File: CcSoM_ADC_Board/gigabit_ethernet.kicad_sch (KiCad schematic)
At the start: 39 parts, among them J5 HR911130A1, U11 RTL8211E-VB-CG, Y1 25MHz

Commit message: changed schottky, began to add digikey part numbers
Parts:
- C1: DigiKey_no (none) -> 1276-CL05B104KP5VPNCCT-ND
- R39, R40: DigiKey_no (none) -> 2019-RK73B1ETTP511JCT-ND
- U11: DigiKey_no (none) -> 1188-SMDICRTL8211E-VB-CG-ND
- Y1: DigiKey_no (none) -> SER4211CT-ND
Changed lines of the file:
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@@
 			)
 		)
+		(property "DigiKey_no" "2019-RK73B1ETTP511JCT-ND"
+			(at 251.46 142.24 90)
+			(effects
+				(font
+					(size 1.27 1.27)
+				)
+				(hide yes)
+			)
+		)
 		(pin "1"
 		)
@@
 			)
 		)
+		(property "DigiKey_no" "SER4211CT-ND "
+			(at 140.97 168.91 90)
+			(effects
+				(font
+					(size 1.27 1.27)
+				)
+				(hide yes)
+			)
+		)
 		(pin "1"
 		)
@@
 			)
 		)
+		(property "DigiKey_no" "2019-RK73B1ETTP511JCT-ND"
+			(at 255.27 129.54 90)
+			(effects
+				(font
+					(size 1.27 1.27)
+				)
+				(hide yes)
+			)
+		)
 		(pin "1"
 		)
@@
 			)
 		)
+		(property "DigiKey_no" "1276-CL05B104KP5VPNCCT-ND"
+			(at 27.94 93.98 0)
+			(effects
+				(font
+					(size 1.27 1.27)
+				)
+				(hide yes)
+			)
+		)
 		(pin "1"
 		)
@@
 			(at 62.23 92.71 0)
 			(effects
+				(font
+					(size 1.27 1.27)
+				)
+				(hide yes)
+			)
+		)
+		(property "DigiKey_no" "1188-SMDICRTL8211E-VB-CG-ND"
+			(at 62.23 92.71 0)
+			(effects

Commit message: digikey no not complete
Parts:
- C32, C33, C34, C35, C36, C37, C38, C39, C40, C48, C49: DigiKey_no (none) -> 399-C0402C104K4RACTUCT-ND
- C50, C53: DigiKey_no (none) -> 490-7203-1-ND
- C51: DigiKey_no (none) -> 399-C0402C103K4RACTUCT-ND
- C52: DigiKey_no (none) -> 478-KGM21AR50J106KUCT-ND
- C54: DigiKey_no (none) -> 478-KGM21NR71E104KTCT-ND
- CA1, CA2: DigiKey_no (none) -> 399-C0402C120J5GACTUCT-ND
- L2: DigiKey_no (none) -> 490-5263-1-ND
- OR1: DigiKey_no (none) -> 311-0.0GRCT-ND
- R25: DigiKey_no (none) -> 541-10.0KLCT-ND
- R26, R27, R28, R29, R32, R35, R37, R38: DigiKey_no (none) -> 541-4.70KLCT-ND
- R33: DigiKey_no (none) -> 541-1.50KLCT-ND
- R34: DigiKey_no (none) -> 541-2.49KLCT-ND
- R36: DigiKey_no (none) -> 541-0.0JCT-ND

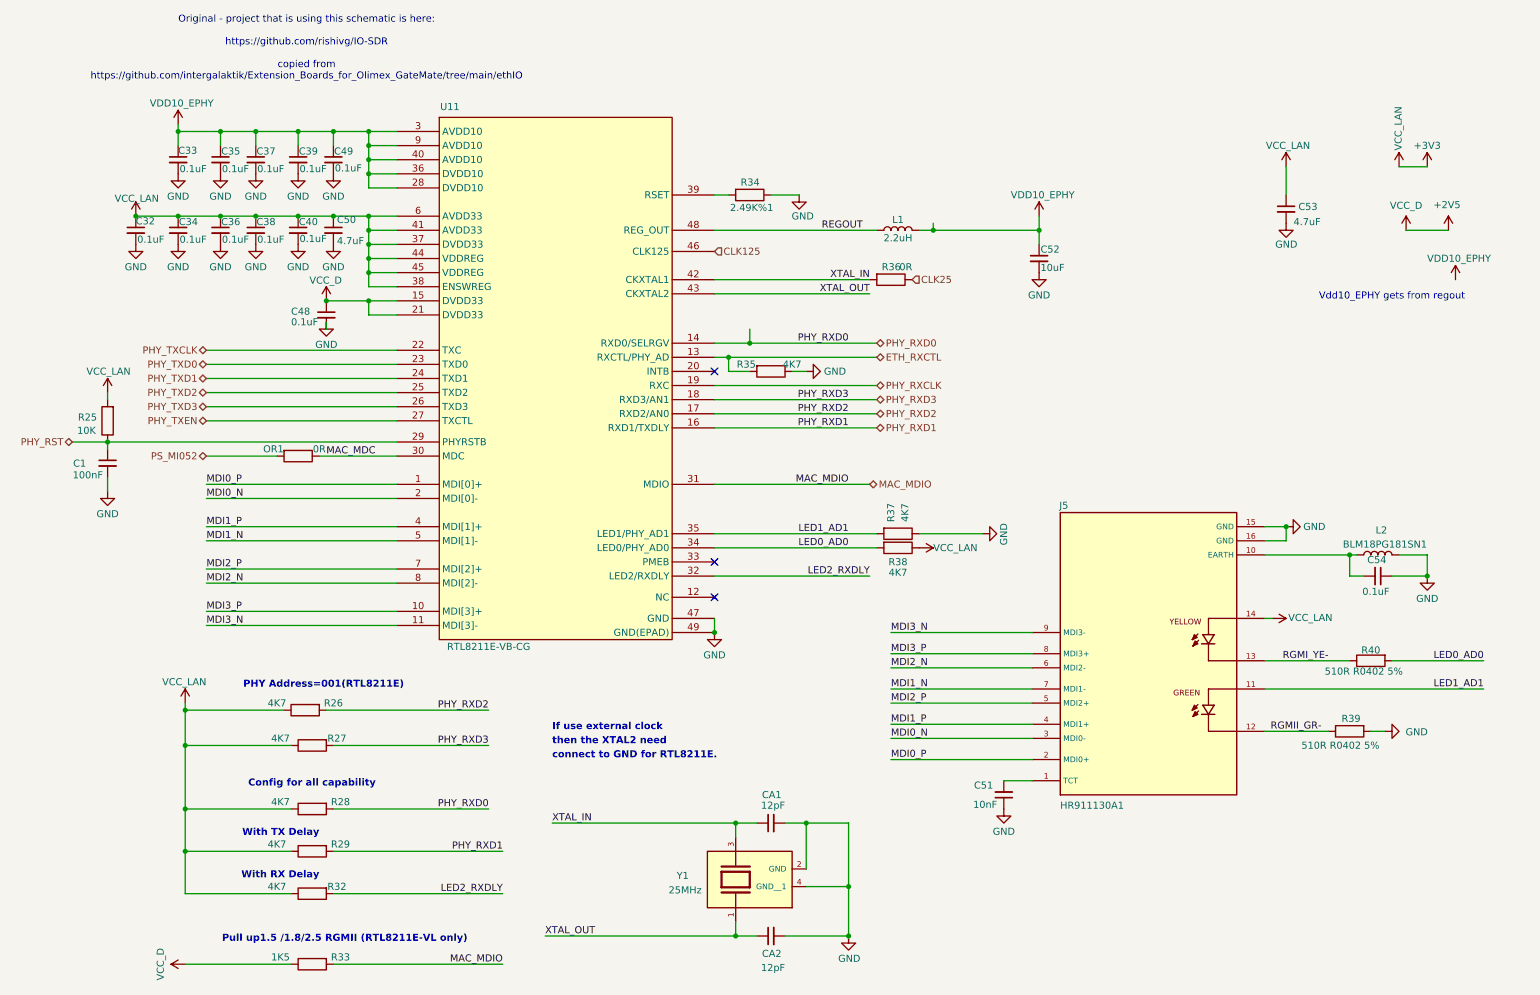
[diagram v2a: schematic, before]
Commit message: changed library path added symbols and footprints
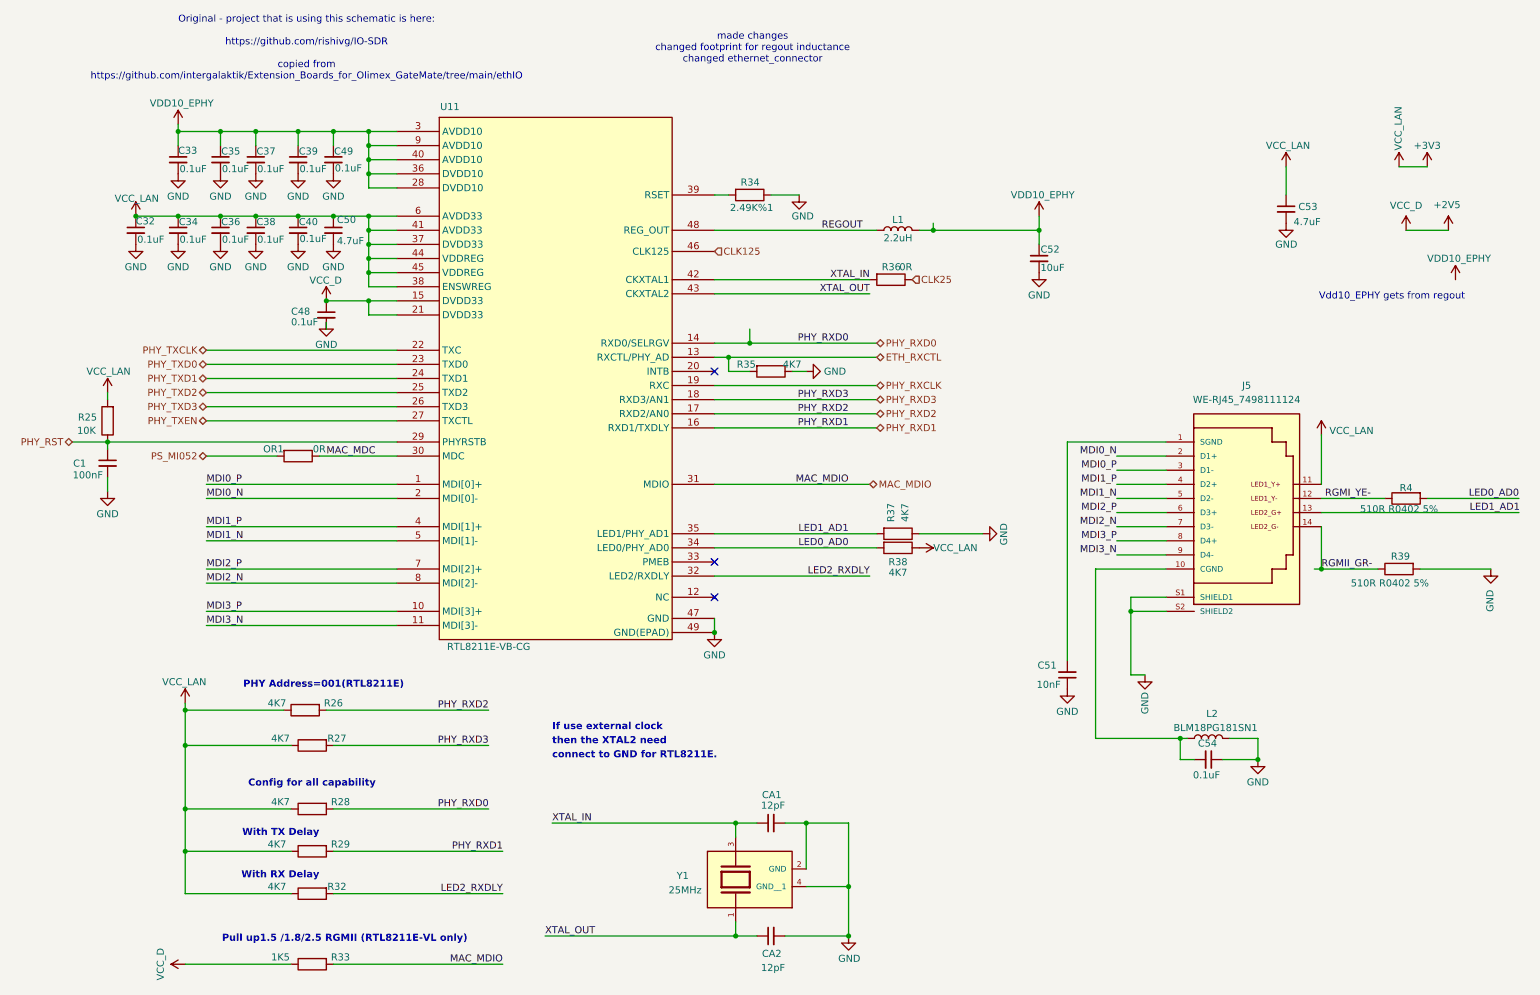
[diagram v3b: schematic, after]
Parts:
- removed J5: HR911130A1, HR911130A1:HR911130A_HAN, symbol PLUTOX_SDR SCH LIB:HR911130A
- removed R40: 510R R0402 5%, Resistor_SMD:R_0402_1005Metric_Pad0.72x0.64mm_HandSolder, symbol Device:R
- added J5: WE-RJ45_7498111124, WE-RJ45_7498111124:7498111124, symbol WE-RJ45_7498111124:WE-RJ45_7498111124
- added R4: 510R R0402 5%, Resistor_SMD:R_0402_1005Metric_Pad0.72x0.64mm_HandSolder, symbol Device:R
- L1: footprint Inductor_SMD:L_0603_1608Metric_Pad1.05x0.95mm_HandSolder -> Inductor_SMD:L_0805_2012Metric_Pad1.05x1.20mm_HandSolder; DigiKey_no (none) -> 535-AOTA-B201210S2R2MTCT-ND
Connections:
- net +3V3: now also J5.11
- net GND: now also J5.S1 (SHIELD1), J5.S2 (SHIELD2)
- net LED0_AD0: now also R4.2
- net LED1_AD1: now also J5.13
- net MDI0_N: now also J5.2 (D1+)
- net MDI0_P: now also J5.3 (D1-)
- net MDI1_N: now also J5.5 (D2-)
- net MDI1_P: now also J5.4 (D2+)
- net MDI2_N: now also J5.7 (D3-)
- net MDI2_P: now also J5.6 (D3+)
- net MDI3_N: now also J5.9 (D4-)
- net MDI3_P: now also J5.8 (D4+)
- net RGMII_GR-: now also J5.14
- net RGMI_YE-: now also J5.12, R4.1
- net at C54.2, L2.2: now also J5.10 (CGND)
- net at C51.2: now also J5.1 (SGND)
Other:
- note added: "made changes changed footprint for regout inductance changed ethernet_connector"
- moved on the sheet: C51, C54, L2, R39

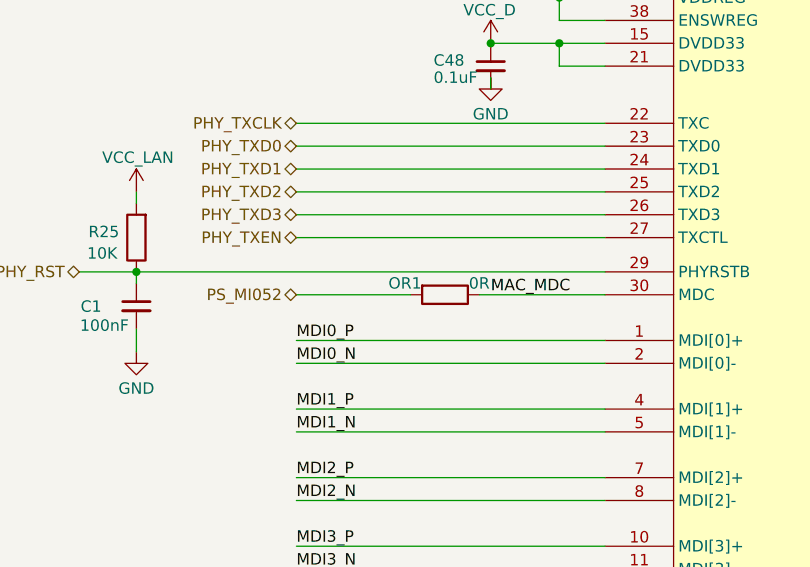
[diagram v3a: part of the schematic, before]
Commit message: corrected differential pairs
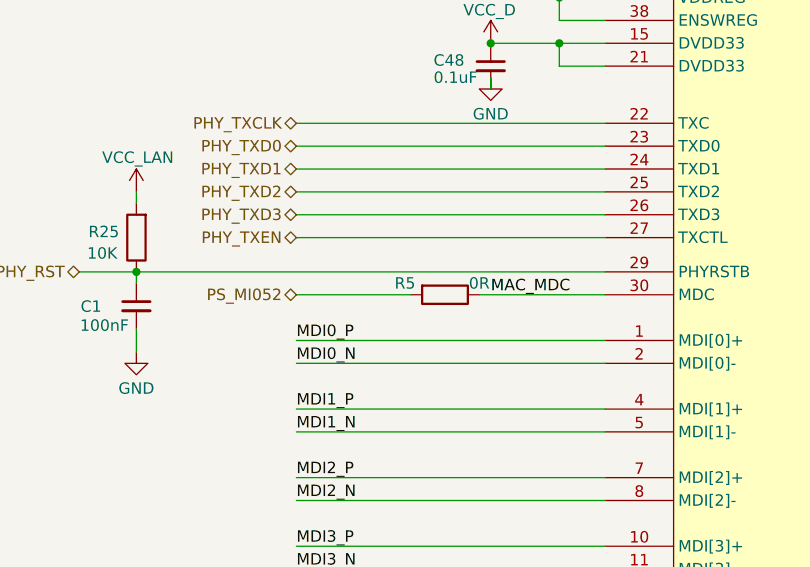
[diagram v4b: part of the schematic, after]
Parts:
- renumbered OR1 to R5
